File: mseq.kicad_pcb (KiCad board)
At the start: 2 copper layers, 116.5 x 69.6 mm, 95 parts, among them J1 Screen_I2C, J3 Conn_ARM_JTAG_SWD_10, SW1 RESET, SW2 ON/OFF, SW3 MS/SLAVE, SW4 BOOT, U1 SN74HCT125DR, U2 H11L1M, U3 AMS1117-3.3, U4 STM32F413CHUx, U5 CP2102N-Axx-xQFN20, U6 H11L1M, U7 W25Q16JVSS, U8 MB85RS256B, Y1 32.768kHz ±20ppm 6pF, Y2 25 MHz ±20ppm 18pF

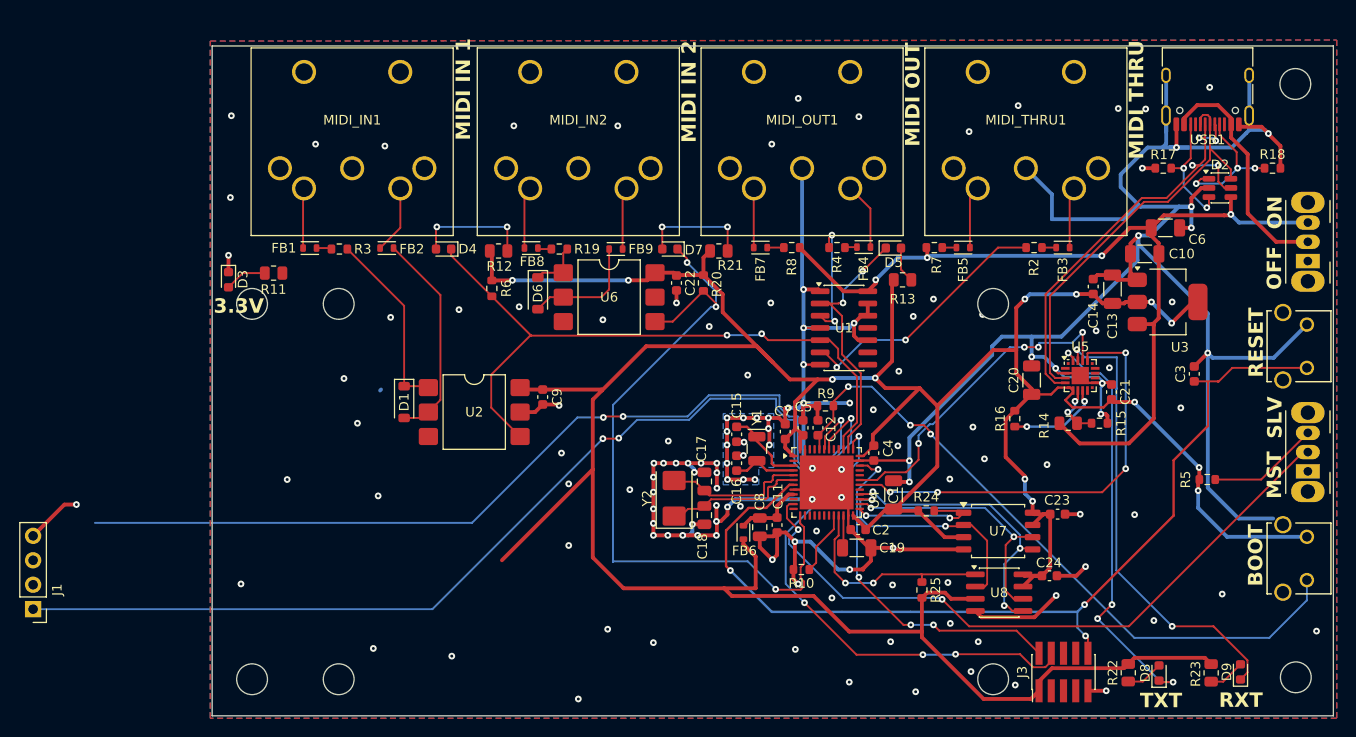
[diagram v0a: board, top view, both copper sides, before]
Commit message: Balance LED brightness, align screen header, pin footprint libraries
- LED series resistors re-sized for roughly equal brightness (~30 mcd):
  R11 green 1k -> 3.9k (C17614), R12/R13/R21 blue 1k -> 390R (C17655),
  R22/R23 orange 1k -> 1.5k (C4310); all UNI-ROYAL 0805 basic parts
- J1 (screen I2C header) moved to y=98.31 so its pins match the
  HS242L03B2C01 OLED module drawing (centred between the 68x39 mm holes)
- fp-lib-table: list the KiCad standard footprint libraries used by the
  board (via ${KICAD10_FOOTPRINT_DIR}) so they are enabled for everyone
- PCB layout work in progress

Co-Authored-By: Claude Opus 5.5 <noreply@anthropic.com>
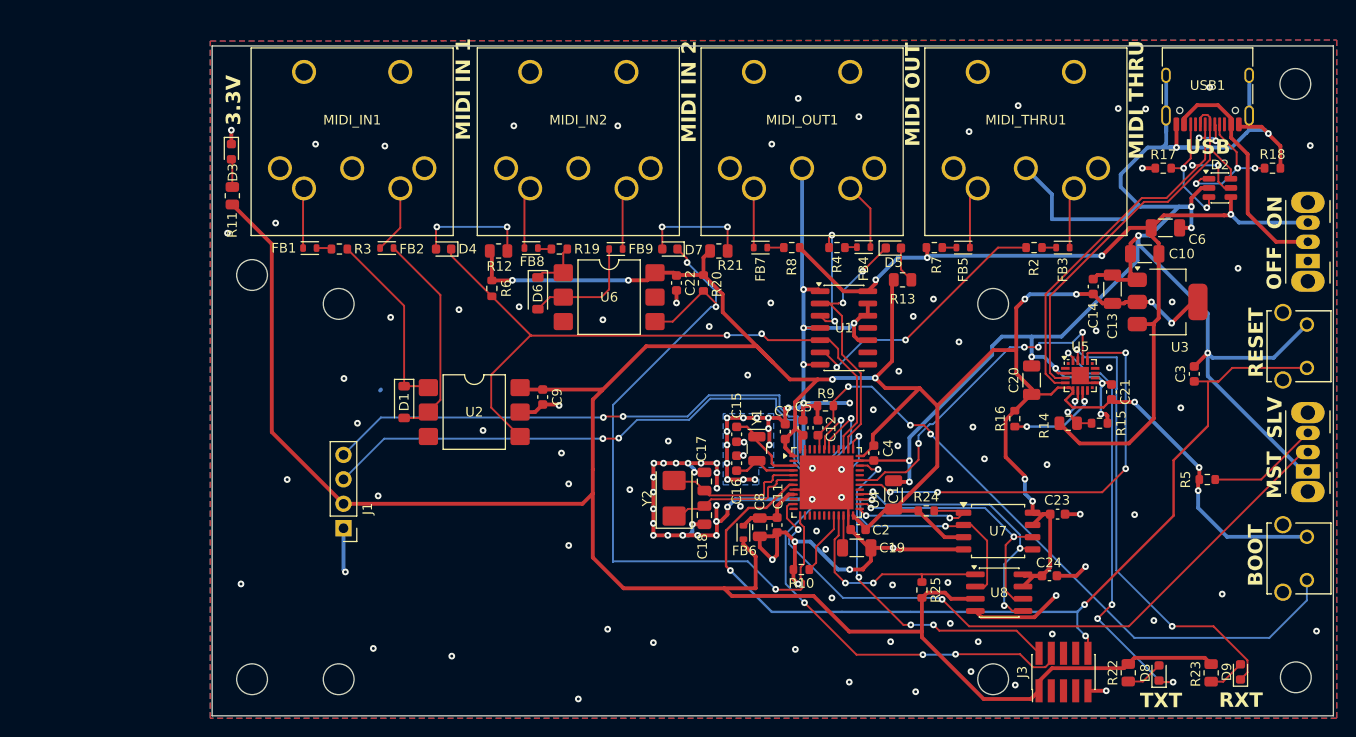
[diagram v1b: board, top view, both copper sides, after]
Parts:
- R11: value 1KR -> 3.9K
- R12, R13, R21: value 1KR -> 390R
- R22, R23: value 1KR -> 1.5K
- moved J1 33.3 mm to (50.5, 98.3)
- moved D3 13.3 mm to (38.9, 59.2)
- moved R11 9.11 mm to (39.0, 63.8), turned to 90 degrees
- moved REF** 3.00 mm to (41.0, 72.0)
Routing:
- net +3.3V: track 385.6 -> 434.5 mm
- net /SCL: track 108.9 -> 71.0 mm
- net /SDA: track 103.4 -> 68.8 mm, vias 4 -> 3
- net Net-(D3-A): track 4.39 -> 2.92 mm
- net GND: track 421.5 -> 420.4 mm, vias 139 -> 145
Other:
- board text added: "USB"

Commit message: Screen header: switch J1 to 5.7 mm female socket
Replace the 8.5 mm BOOMELE socket (C2718488) with the hanxia
HX PM2.54-1x4P ZC H5.7 (C46061763) to lower the screen stack-up.
Use the PinSocket_1x04 footprint instead of the male PinHeader one
(identical pads) and add Connector_PinSocket_2.54mm to fp-lib-table.

Co-Authored-By: Claude Opus 5.5 <noreply@anthropic.com>
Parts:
- J1: footprint Connector_PinHeader_2.54mm:PinHeader_1x04_P2.54mm_Vertical -> Connector_PinSocket_2.54mm:PinSocket_1x04_P2.54mm_Vertical
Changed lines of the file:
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@@
 		)
 	)
-	(footprint "Connector_PinHeader_2.54mm:PinHeader_1x04_P2.54mm_Vertical"
+	(footprint "Connector_PinSocket_2.54mm:PinSocket_1x04_P2.54mm_Vertical"
 		(layer "F.Cu")
 		(at 50.5 98.31 180)
-		(descr "Through hole straight pin header, 1x04, 2.54mm pitch, single row")
-		(tags "Through hole pin header THT 1x04 2.54mm single row")
+		(descr "Through hole straight socket strip, 1x04, 2.54mm pitch, single row (from Kicad 4.0.7), script generated")
+		(tags "Through hole socket strip THT 1x04 2.54mm single row")
 		(property "Reference" "J1"
 			(at -2.5 2.02 90)
@@
 			)
 		)
-		(property "LCSC" "C2718488"
+		(property "LCSC" "C46061763"
 			(at 0 0 180)
 			(unlocked yes)
@@
 			)
 		)
-		(property "MPN" "2.54-1*4P"
+		(property "MPN" "HX PM2.54-1x4P ZC H5.7"
 			(at 0 0 180)
 			(unlocked yes)
@@
 		(duplicate_pad_numbers_are_jumpers no)
 		(fp_line
-			(start 1.38 1.27)
-			(end 1.38 9)
-			(stroke
-				(width 0.12)
-				(type solid)
-			)
-			(layer "F.SilkS")
-		)
-		(fp_line
-			(start -1.38 9)
-			(end 1.38 9)
-			(stroke
-				(width 0.12)
-				(type solid)
-			)
-			(layer "F.SilkS")
-		)
-		(fp_line
-			(start -1.38 1.27)
-			(end 1.38 1.27)
-			(stroke
-				(width 0.12)
-				(type solid)
-			)
-			(layer "F.SilkS")
-		)
-		(fp_line
-			(start -1.38 1.27)
-			(end -1.38 9)
-			(stroke
-				(width 0.12)
-				(type solid)
-			)
-			(layer "F.SilkS")
-		)
-		(fp_line
-			(start -1.38 0)
-			(end -1.38 -1.38)
-			(stroke
-				(width 0.12)
-				(type solid)
-			)
-			(layer "F.SilkS")
-		)
-		(fp_line
-			(start -1.38 -1.38)
-			(end 0 -1.38)
-			(stroke
-				(width 0.12)
-				(type solid)
-			)
-			(layer "F.SilkS")
-		)
-		(fp_rect
+			(start -1.33 1.27)
+			(end -1.33 8.95)
+			(stroke
+				(width 0.12)
+				(type solid)
+			)
+			(layer "F.SilkS")
+		)
+		(fp_line
+			(start -1.33 1.27)
+			(end 1.33 1.27)
+			(stroke
+				(width 0.12)
+				(type solid)
+			)
+			(layer "F.SilkS")
+		)
+		(fp_line
+			(start -1.33 8.95)
+			(end 1.33 8.95)
+			(stroke
+				(width 0.12)
+				(type solid)
+			)
+			(layer "F.SilkS")
+		)
+		(fp_line
+			(start 0 -1.33)
+			(end 1.33 -1.33)
+			(stroke
+				(width 0.12)
+				(type solid)
+			)
+			(layer "F.SilkS")
+		)
+		(fp_line
+			(start 1.33 -1.33)
+			(end 1.33 0)
+			(stroke
+				(width 0.12)
+				(type solid)
+			)
+			(layer "F.SilkS")
+		)
+		(fp_line
+			(start 1.33 1.27)
+			(end 1.33 8.95)
+			(stroke
+				(width 0.12)
+				(type solid)
+			)
+			(layer "F.SilkS")
+		)
+		(fp_line
 			(start -1.77 -1.77)
+			(end 1.77 -1.77)
+			(stroke
+				(width 0.05)
+				(type solid)
+			)
+			(layer "F.CrtYd")
+		)
+		(fp_line
+			(start -1.77 9.39)
+			(end -1.77 -1.77)
+			(stroke
+				(width 0.05)
+				(type solid)
+			)
+			(layer "F.CrtYd")
+		)
+		(fp_line
+			(start 1.77 -1.77)
 			(end 1.77 9.39)
 			(stroke
@@
 				(type solid)
 			)
-			(fill no)
-			(layer "F.CrtYd")
+			(layer "F.CrtYd")
+		)
+		(fp_line
+			(start 1.77 9.39)
+			(end -1.77 9.39)
+			(stroke
+				(width 0.05)
+				(type solid)
+			)
+			(layer "F.CrtYd")
+		)
+		(fp_line
+			(start -1.27 -1.27)
+			(end 0.635 -1.27)
+			(stroke
+				(width 0.1)
+				(type solid)
+			)
+			(layer "F.Fab")
+		)
+		(fp_line
+			(start -1.27 8.89)
+			(end -1.27 -1.27)
+			(stroke
+				(width 0.1)
+				(type solid)
+			)
+			(layer "F.Fab")
+		)
+		(fp_line
+			(start 0.635 -1.27)
+			(end 1.27 -0.635)
+			(stroke
+				(width 0.1)
+				(type solid)
+			)
+			(layer "F.Fab")
+		)
+		(fp_line
+			(start 1.27 -0.635)
+			(end 1.27 8.89)
+			(stroke
+				(width 0.1)
+				(type solid)
+			)
+			(layer "F.Fab")
 		)
 		(fp_line
@@
 			(layer "F.Fab")
 		)
-		(fp_line
-			(start 1.27 -1.27)
-			(end 1.27 8.89)
-			(stroke
-				(width 0.1)
-				(type solid)
-			)
-			(layer "F.Fab")
-		)
-		(fp_line
-			(start -0.635 -1.27)
-			(end 1.27 -1.27)
-			(stroke
-				(width 0.1)
-				(type solid)
-			)
-			(layer "F.Fab")
-		)
-		(fp_line
-			(start -1.27 8.89)
-			(end -1.27 -0.635)
-			(stroke
-				(width 0.1)
-				(type solid)
-			)
-			(layer "F.Fab")
-		)
-		(fp_line
-			(start -1.27 -0.635)
-			(end -0.635 -1.27)
-			(stroke
-				(width 0.1)
-				(type solid)
-			)
-			(layer "F.Fab")
-		)
 		(fp_text user "${REFERENCE}"
 			(at 0 3.81 90)
@@
 		)
 		(embedded_fonts no)
-		(model "${KICAD10_3DMODEL_DIR}/Connector_PinHeader_2.54mm.3dshapes/PinHeader_1x04_P2.54mm_Vertical.step"
+		(model "${KICAD10_3DMODEL_DIR}/Connector_PinSocket_2.54mm.3dshapes/PinSocket_1x04_P2.54mm_Vertical.step"
 			(offset
 				(xyz 0 0 0)
